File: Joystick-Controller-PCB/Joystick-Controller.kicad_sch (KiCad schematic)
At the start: 13 parts, among them J1 Conn_01x28_Socket, J2 Conn_01x28_Socket, J3 Conn_01x03_Socket, J4 Conn_01x04_Socket, SW1 SW_Push

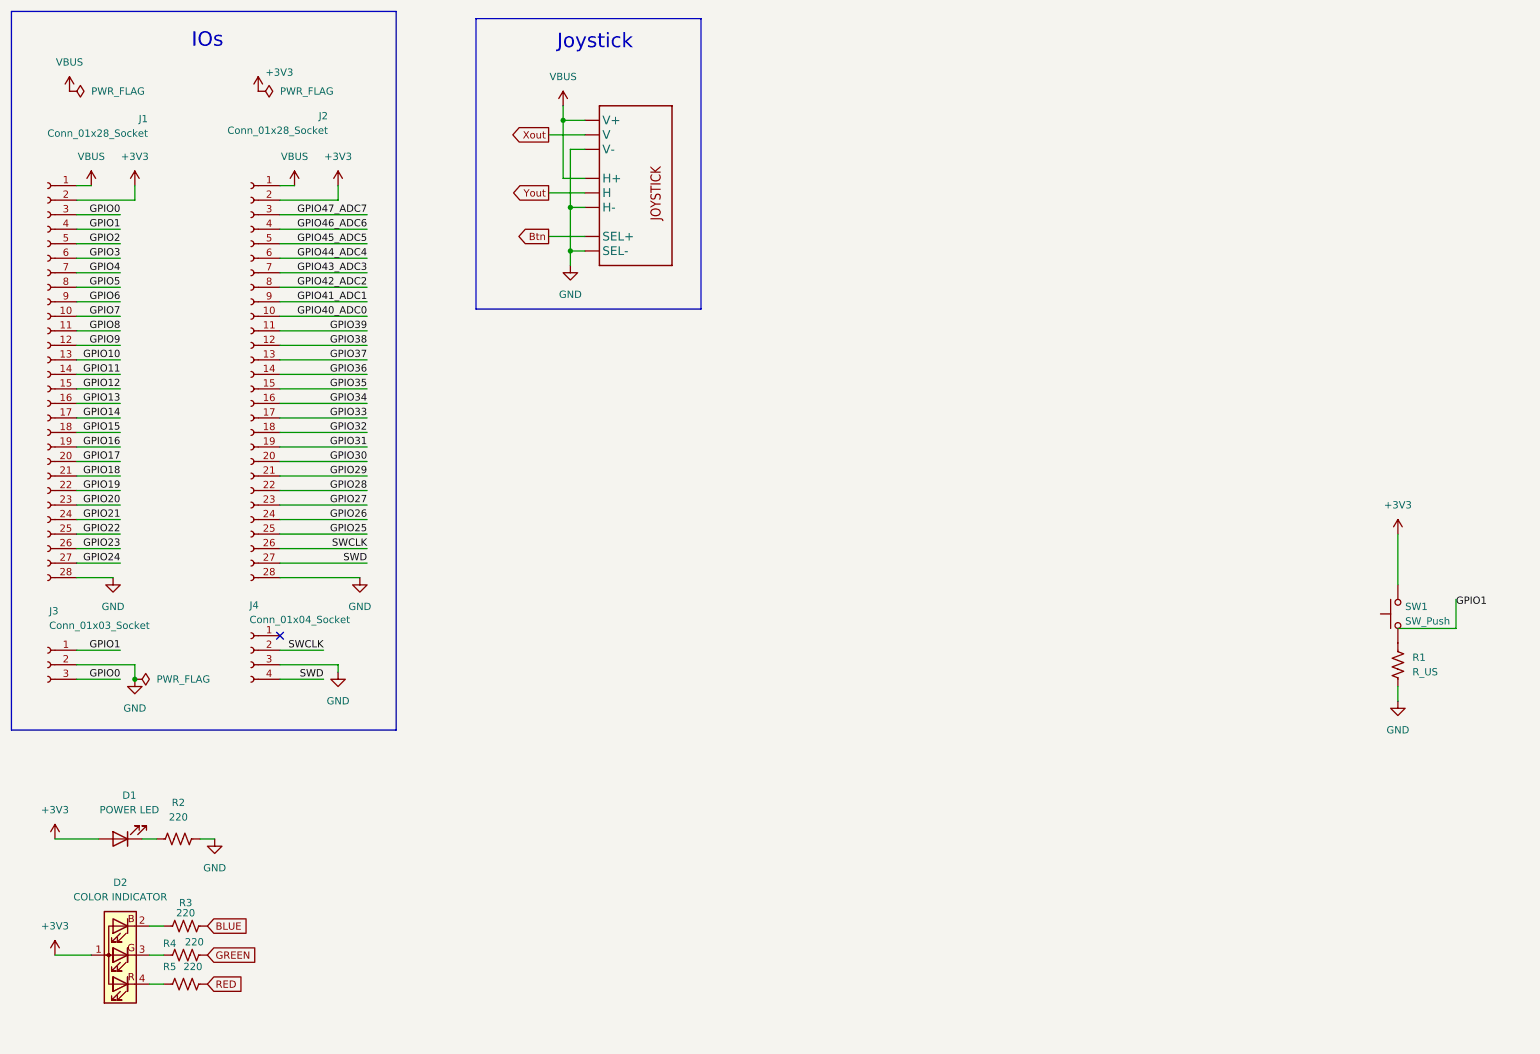
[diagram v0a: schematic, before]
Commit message: Added TFT schematics
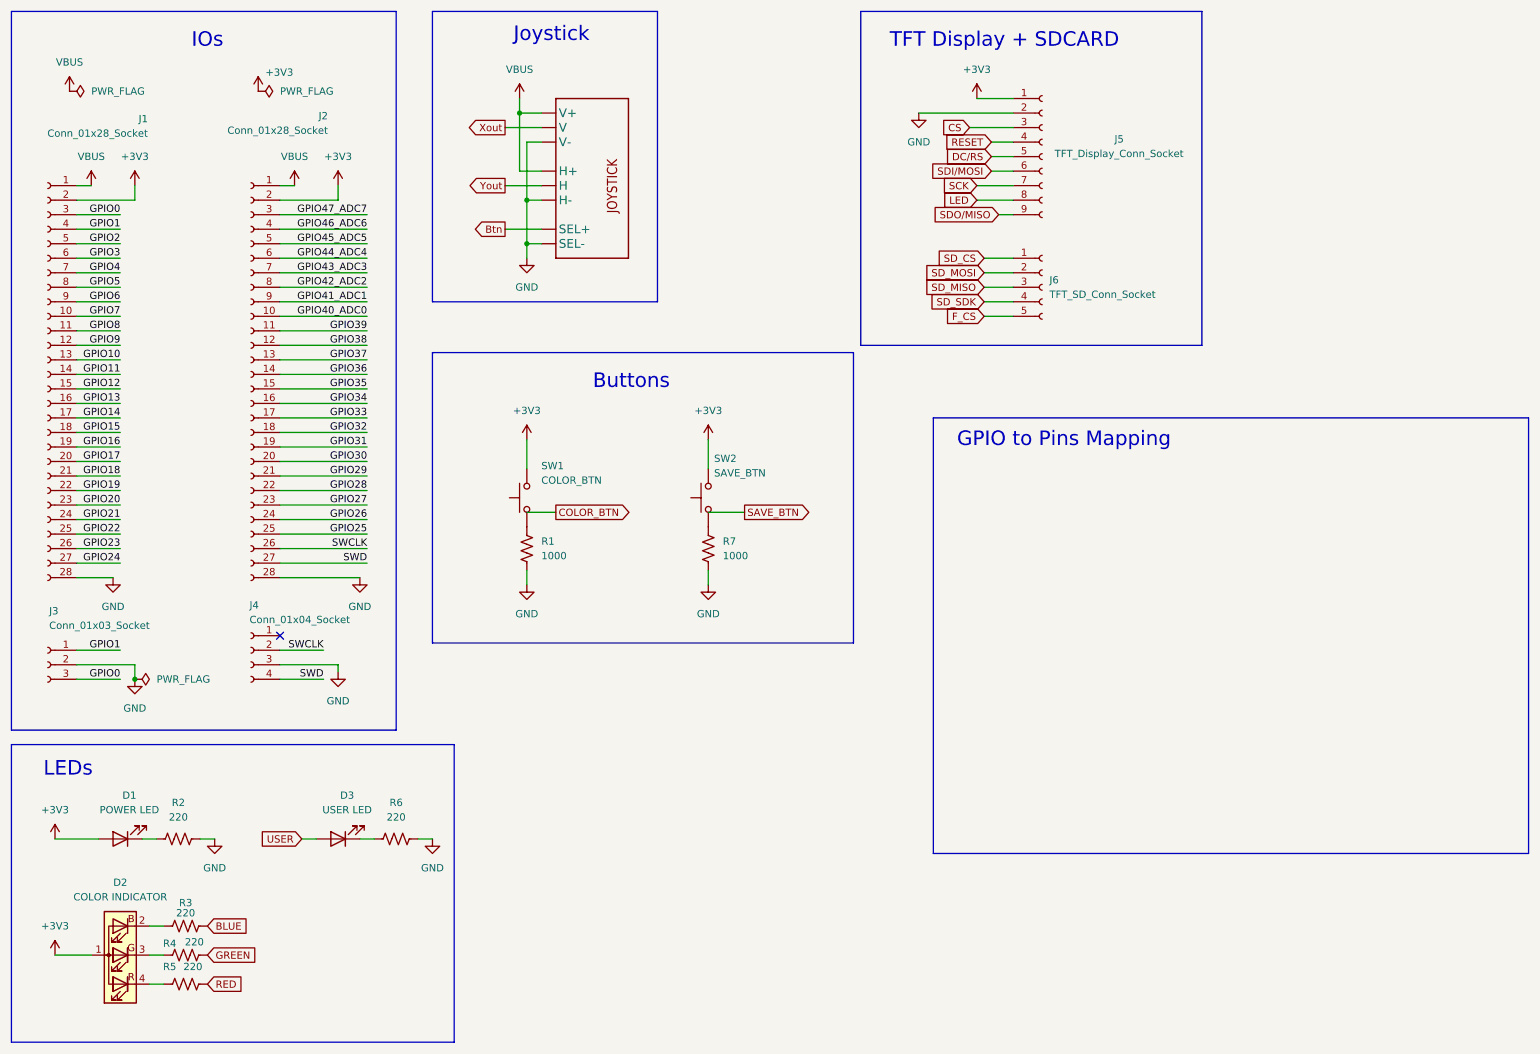
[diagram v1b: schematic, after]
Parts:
- added D3: USER LED, symbol Device:LED
- added J5: TFT_Display_Conn_Socket, symbol Connector:Conn_01x09_Socket
- added J6: TFT_SD_Conn_Socket, symbol Connector:Conn_01x05_Socket
- added R6: 220, symbol Device:R_US
- added R7: 1000, symbol Device:R_US
- added SW2: SAVE_BTN, symbol Switch:SW_Push
- R1: value R_US -> 1000
- SW1: value SW_Push -> COLOR_BTN
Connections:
- net +3V3: now also J5.1 (Pin_1), SW2.2
- net GND: now also J5.2 (Pin_2), R6.2, R7.2
- new net: D3.1 (K), R6.1
- new net: R7.1, SW2.1
- new net CS: J5.3 (Pin_3)
- new net DC/RS: J5.5 (Pin_5)
- new net F_CS: J6.5 (Pin_5)
- new net LED: J5.8 (Pin_8)
- new net RESET: J5.4 (Pin_4)
- new net SCK: J5.7 (Pin_7)
- new net SDI/MOSI: J5.6 (Pin_6)
- new net SDO/MISO: J5.9 (Pin_9)
- new net SD_CS: J6.1 (Pin_1)
- new net SD_MISO: J6.3 (Pin_3)
- new net SD_MOSI: J6.2 (Pin_2)
- new net SD_SDK: J6.4 (Pin_4)
- new net USER: D3.2 (A)
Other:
- note added: "Buttons"
- note added: "GPIO to Pins Mapping"
- note added: "LEDs"
- note added: "TFT Display + SDCARD"
- moved on the sheet: R1, SW1

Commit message: Mapped GPIO pins to functions. Schematic ready for PCB design
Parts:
- added C1: 0.1uF, symbol Device:C_Small
- added C2: 10uF, symbol Device:C_Polarized_US
- added R8: 10k, symbol Device:R_US
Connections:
- net BLUE is gone; now on net GPIO3: R3.2
- net Btn is gone; now on net GPIO20: U1.B1A (SEL+)
- net CS is gone; now on net GPIO17: J5.3 (Pin_3)
- net DC/RS is gone; now on net GPIO16: J5.5 (Pin_5)
- net GREEN is gone; now on net GPIO4: R4.2
- net LED is gone; now on net +3V3: J5.8 (Pin_8)
- net RED is gone; now on net GPIO5: R5.2
- net RESET is gone; now on net GPIO15: J5.4 (Pin_4)
- net SCK is gone; now on net GPIO18: J5.7 (Pin_7)
- net SDI/MOSI is gone; now on net GPIO19: J5.6 (Pin_6)
- net SD_CS is gone; now on net GPIO29: J6.1 (Pin_1)
- net SD_MOSI is gone; now on net GPIO31: J6.2 (Pin_2)
- net SD_SDK is gone; now on net GPIO30: J6.4 (Pin_4)
- net USER is gone; now on net GPIO2: D3.2 (A)
- net Xout is gone; now on net GPIO40_ADC0: U1.V2 (V)
- net Yout is gone; now on net GPIO41_ADC1: U1.H2 (H)
- net +3V3: now also C1.2, C2.1, R8.1
- net GND: now also C1.1, C2.2
- net GPIO38: now also R7.1, SW2.1
- net GPIO39: now also R1.1, SW1.1
- net F_CS: no longer names the net of J6.5 (Pin_5)
- net SDO/MISO: no longer names the net of J5.9 (Pin_9)
- net SD_MISO: no longer names the net of J6.3 (Pin_3)
- net SD_MISO: now also R8.2
- no-connect marks 1 -> 33
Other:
- note added: "Button"
- note added: "DC/RS"
- note added: "FLASH_CS"
- note added: "GND"
- note added: "LED"
- note added: "RESET"
- note added: "SDO(MISO)"
- note added: "SD_CS"
- note added: "SD_MISO"
- note added: "SD_MOSI"
- note added: "SD_SDK"
- note added: "SPI0_CS"
- note added: "SPI0_SCK"
- note added: "SPI0_TX"
- note added: "VDD"
- note added: "X-pos"
- note added: "Y-pos"
- note removed: "GPIO to Pins Mapping"
- moved on the sheet: J5, J6, R1, R7, SW1, SW2

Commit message: Placement done
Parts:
- removed SW1: COLOR_BTN, symbol Switch:SW_Push
- removed SW2: SAVE_BTN, symbol Switch:SW_Push
- added SW1, SW3: COM-10302, footprints:COM-10302_SPK, symbol COM-10302:COM-10302
- C1, C2: footprint (none) -> Capacitor_Tantalum_SMD:CP_EIA-2012-12_Kemet-R_HandSolder
- D1: footprint (none) -> Diode_SMD:D_0805_2012Metric_Pad1.15x1.40mm_HandSolder
- D2: footprint (none) -> LED_SMD:LED_RGB_5050-6
- D3: footprint (none) -> LED_SMD:LED_0603_1608Metric_Pad1.05x0.95mm_HandSolder
- J1, J2: footprint (none) -> Connector_PinSocket_2.54mm:PinSocket_1x28_P2.54mm_Vertical
- J3: footprint (none) -> Connector_PinSocket_2.54mm:PinSocket_1x03_P2.54mm_Vertical
- J4: footprint (none) -> Connector_PinSocket_2.54mm:PinSocket_1x04_P2.54mm_Vertical
- J5: footprint (none) -> Connector_PinSocket_2.54mm:PinSocket_1x09_P2.54mm_Vertical
- J6: footprint (none) -> Connector_PinSocket_2.54mm:PinSocket_1x05_P2.54mm_Vertical
- R1, R2, R3, R4, R5, R6, R7, R8: footprint (none) -> Resistor_SMD:R_0805_2012Metric_Pad1.20x1.40mm_HandSolder
- U1: footprint joystick:JOYSTICK -> footprints2:XDCR_COM-09032
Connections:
- net +3V3: now also SW1.4, SW3.4
- net GPIO3: now also R5.2; no longer R3.2
- net GPIO38: now also SW1.2
- net GPIO39: now also SW3.2
- net GPIO5: now also R3.2; no longer R5.2
- no-connect marks 33 -> 37
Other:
- moved on the sheet: R1, R7

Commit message: Iteration 1
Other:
- moved on the sheet: SW1
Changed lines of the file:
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@@
 	)
 	(junction
-		(at 233.68 33.02)
+		(at 152.4 121.92)
 		(diameter 0)
 		(color 0 0 0 0)
 	)
 	(junction
-		(at 222.25 38.1)
+		(at 233.68 33.02)
 		(diameter 0)
 		(color 0 0 0 0)
 	)
 	(junction
-		(at 152.4 121.92)
+		(at 222.25 38.1)
 		(diameter 0)
 		(color 0 0 0 0)
@@
 	)
 	(junction
-		(at 114.3 121.92)
+		(at 114.3 123.19)
 		(diameter 0)
 		(color 0 0 0 0)
@@
 	)
 	(no_connect
-		(at 152.4 101.6)
+		(at 152.4 100.33)
 	)
 	(no_connect
@@
 	)
 	(no_connect
-		(at 149.86 101.6)
+		(at 149.86 100.33)
 	)
 	(no_connect
@@
 	(wire
 		(pts
-			(xy 114.3 123.19) (xy 114.3 121.92)
-		)
-		(stroke
-			(width 0)
-			(type default)
-		)
-	)
-	(wire
-		(pts
 			(xy 87.63 160.02) (xy 90.17 160.02)
 		)
@@
 	(wire
 		(pts
-			(xy 143.51 121.92) (xy 149.86 121.92)
+			(xy 143.51 120.65) (xy 149.86 120.65)
 		)
 		(stroke
@@
 	(wire
 		(pts
-			(xy 114.3 121.92) (xy 114.3 120.65)
+			(xy 114.3 123.19) (xy 114.3 121.92)
 		)
 		(stroke
@@
 	(wire
 		(pts
+			(xy 152.4 120.65) (xy 152.4 121.92)
+		)
+		(stroke
+			(width 0)
+			(type default)
+		)
+	)
+	(wire
+		(pts
 			(xy 116.84 60.96) (xy 135.89 60.96)
 		)
@@
 	(wire
 		(pts
-			(xy 152.4 121.92) (xy 152.4 120.65)
-		)
-		(stroke
-			(width 0)
-			(type default)
-		)
-	)
-	(wire
-		(pts
 			(xy 133.35 55.88) (xy 135.89 55.88)
 		)
@@
 	(wire
 		(pts
-			(xy 114.3 121.92) (xy 130.81 121.92)
+			(xy 114.3 123.19) (xy 130.81 123.19)
 		)
 		(stroke
@@
 	(wire
 		(pts
-			(xy 143.51 116.84) (xy 143.51 121.92)
+			(xy 143.51 116.84) (xy 143.51 120.65)
 		)
 		(stroke
@@
 	)
 	(label "GPIO39"
-		(at 130.81 121.92 180)
+		(at 130.81 123.19 180)
 		(effects
 			(font
@@
 	(symbol
 		(lib_id "COM-10302:COM-10302")
-		(at 152.4 101.6 270)
+		(at 152.4 100.33 270)
 		(unit 1)
 		(exclude_from_sim no)
@@
 		(fields_autoplaced yes)
 		(property "Reference" "SW1"
-			(at 156.21 110.4899 90)
+			(at 156.21 109.2199 90)
 			(effects
 				(font
@@
 		)
 		(property "Value" "COM-10302"
-			(at 156.21 113.0299 90)
+			(at 156.21 111.7599 90)
 			(effects
 				(font
@@
 		)
 		(property "Footprint" "footprints:COM-10302_SPK"
-			(at 152.4 101.6 0)
+			(at 152.4 100.33 0)
 			(effects
 				(font
@@
 		)
 		(property "Datasheet" "COM-10302"
-			(at 152.4 101.6 0)
+			(at 152.4 100.33 0)
 			(effects
 				(font
@@
 		)
 		(property "Description" ""
-			(at 152.4 101.6 0)
+			(at 152.4 100.33 0)
 			(effects
 				(font

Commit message: pcb files checked by Niraj
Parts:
- R1, R7: value 1000 -> 10k
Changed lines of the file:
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@@
 			)
 		)
-		(property "Value" "1000"
+		(property "Value" "10k"
 			(at 154.94 128.2699 0)
 			(effects
@@
 			)
 		)
-		(property "Value" "1000"
+		(property "Value" "10k"
 			(at 116.84 128.2699 0)
 			(effects

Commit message: Board Complete
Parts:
- removed SW1, SW3: COM-10302, footprints:COM-10302_SPK, symbol COM-10302:COM-10302
- added S1, S2: B3F-4055, B3F-4055:SW_B3F-4055, symbol B3F:B3F-4055
- R2, R3, R4, R5, R6: value 220 -> 100
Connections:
- net +3V3: now also S1.1, S1.2, S2.1, S2.2
- net GPIO38: now also S2.3, S2.4
- net GPIO39: now also S1.3, S1.4
- no-connect marks 37 -> 33
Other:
- moved on the sheet: R1

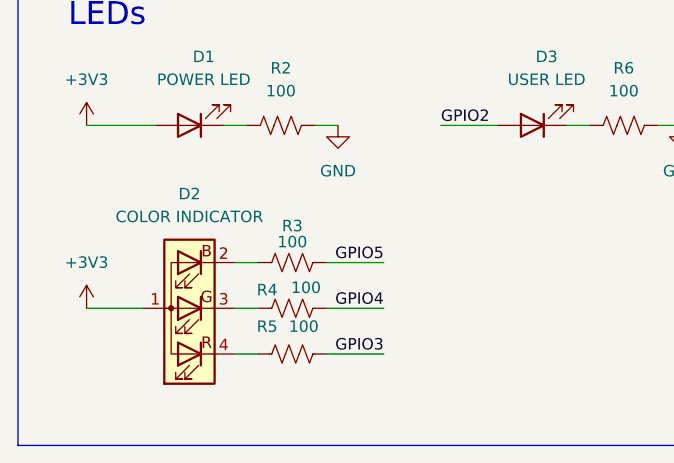
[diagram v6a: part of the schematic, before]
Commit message: Updated LED part and resistor values. Added footprint for switch and RGB LED
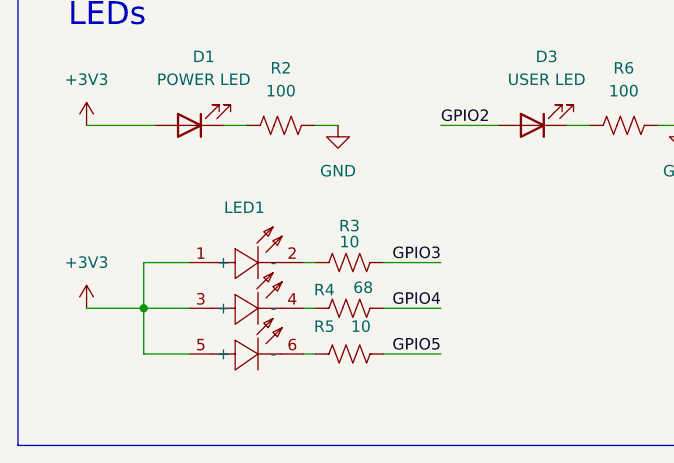
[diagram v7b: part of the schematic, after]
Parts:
- removed D2: COLOR INDICATOR, LED_SMD:LED_RGB_5050-6, symbol Device:LED_ABGR
- added LED1: ~, ProLib_pcs_2025-11-13:LED-SMD_6PIN-L1.60-W1.50-BL-RD, symbol SMD-6P,1.6x1.5mm RGB LEDs:E6C1615RGBC3UDA
- R3, R5: value 100 -> 10
- R4: value 100 -> 68
- S1, S2: footprint B3F-4055:SW_B3F-4055 -> B3F_4055:SW_B3F-4055
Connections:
- net +3V3: now also LED1.1 (+), LED1.3 (+), LED1.5 (+)
- net GPIO3: now also R3.2; no longer R5.2
- net GPIO5: now also R5.2; no longer R3.2
- net at R3.1: now also LED1.2 (-)
- net at R4.1: now also LED1.4 (-)
- net at R5.1: now also LED1.6 (-)
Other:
- moved on the sheet: R3, R4, R5

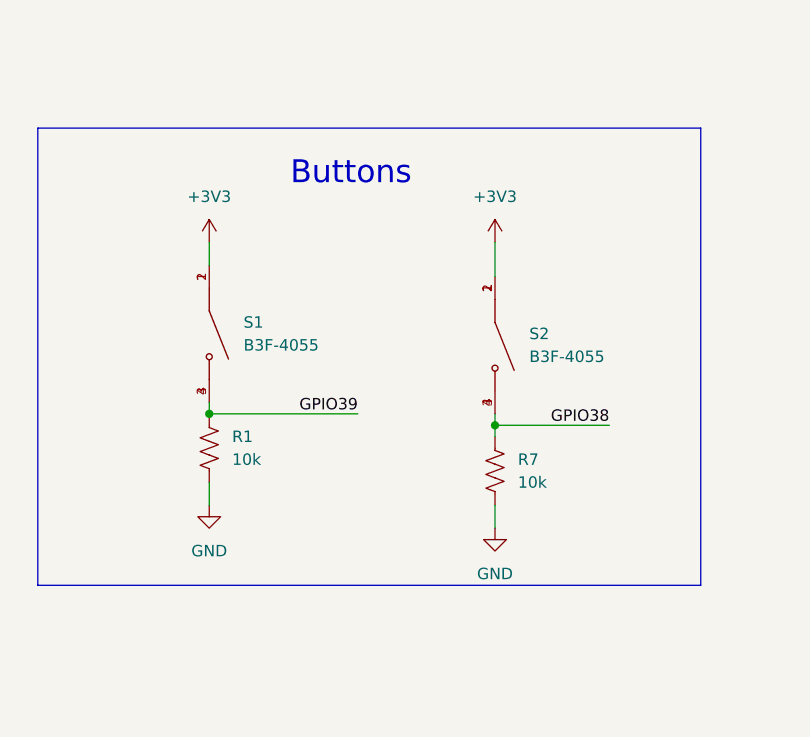
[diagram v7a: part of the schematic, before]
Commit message: Changed buttons to active-low
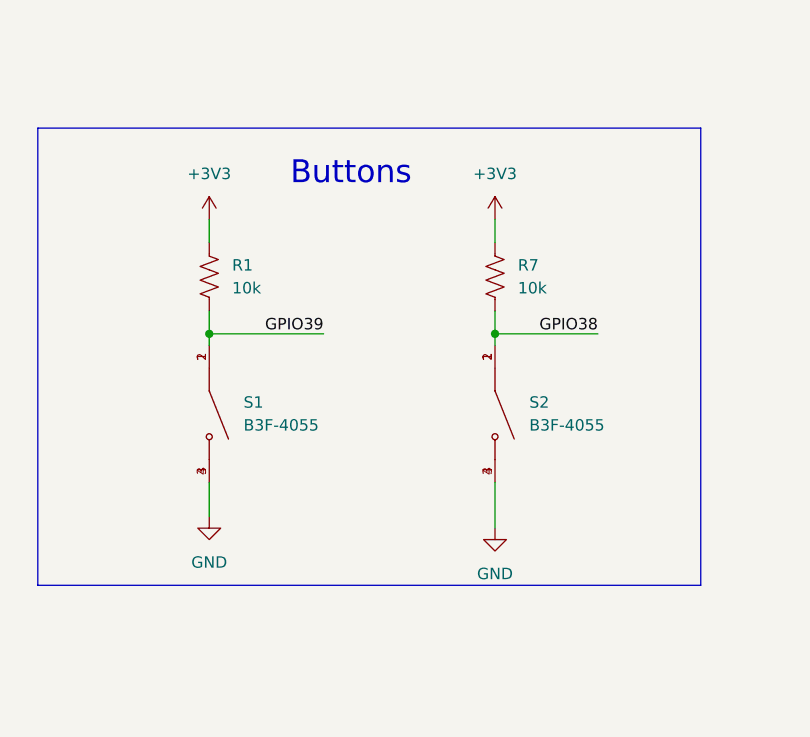
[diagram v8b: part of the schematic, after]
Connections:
- net +3V3: now also R1.1, R7.1; no longer S1.1, S1.2, S2.1, S2.2
- net GND: now also S1.3, S1.4, S2.3, S2.4; no longer R1.2, R7.2
- net GPIO38: now also R7.2, S2.1, S2.2; no longer R7.1, S2.3, S2.4
- net GPIO39: now also R1.2, S1.1, S1.2; no longer R1.1, S1.3, S1.4
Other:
- moved on the sheet: R1, R7, S1, S2
